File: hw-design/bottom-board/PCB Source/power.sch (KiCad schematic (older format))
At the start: 19 parts, among them J1 Power Jack, J2 HMI_POWER, U1 MURATA 5V, U2 LD1117S50TR_SOT223

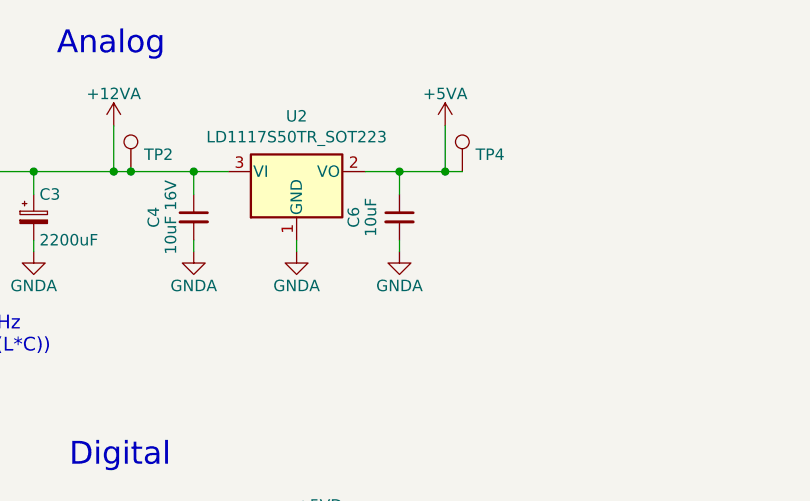
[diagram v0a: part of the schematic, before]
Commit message: change bias voltages to 5V, isolate input GND connections
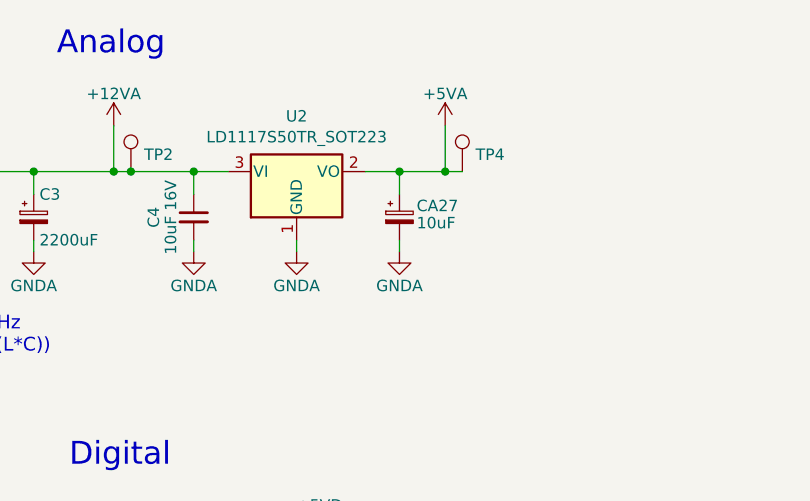
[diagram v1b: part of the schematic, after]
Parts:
- removed C6: 10uF, Capacitor_SMD:C_0603_1608Metric, symbol bottom-board-rescue:C_Small-Device
- added CA27: 10uF, Capacitor_SMD:CP_Elec_4x5.7, symbol bottom-board-rescue:CP_Small-Device
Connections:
- net +5VA: now also CA27.1
- net GND: now also CA27.2
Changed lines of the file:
@@
 Wire Wire Line
 	5900 1950 6100 1950
-$Comp
-L bottom-board-rescue:C_Small-Device C6
-U 1 1 5B5D1557
-P 5900 2150
-F 0 "C6" V 5700 2150 50  0000 C CNN
-F 1 "10uF" V 5775 2150 50  0000 C CNN
-F 2 "Capacitor_SMD:C_0603_1608Metric" H 5900 2150 60  0001 C CNN
-F 3 "" H 5900 2150 60  0000 C CNN
-F 4 "CL10A106MQ8NNNC" H 600 -3200 50  0001 C CNN "MPN"
-	1    5900 2150
-	1    0    0    -1
-$EndComp
 Text Notes 3650 2750 0    60   ~ 0
 LPF Fc=107Hz\n1/(2*pi*sqrt(L*C))
@@
 Wire Wire Line
 	8750 5300 8800 5300
+$Comp
+L bottom-board-rescue:CP_Small-Device CA?
+U 1 1 5FDC0C8E
+P 5900 2150
+AR Path="/54F72C8D/5FDC0C8E" Ref="CA?"  Part="1"
+AR Path="/54F7244B/5FDC0C8E" Ref="CA27"  Part="1"
+F 0 "CA27" H 5975 2200 50  0000 L CNN
+F 1 "10uF" H 5975 2125 50  0000 L CNN
+F 2 "Capacitor_SMD:CP_Elec_4x5.7" H 5900 2150 60  0001 C CNN
+F 3 "" H 5900 2150 60  0000 C CNN
+F 4 "EEE-HB1C100R" H 800 650 50  0001 C CNN "MPN"
+	1    5900 2150
+	1    0    0    -1
+$EndComp
 $EndSCHEMATC

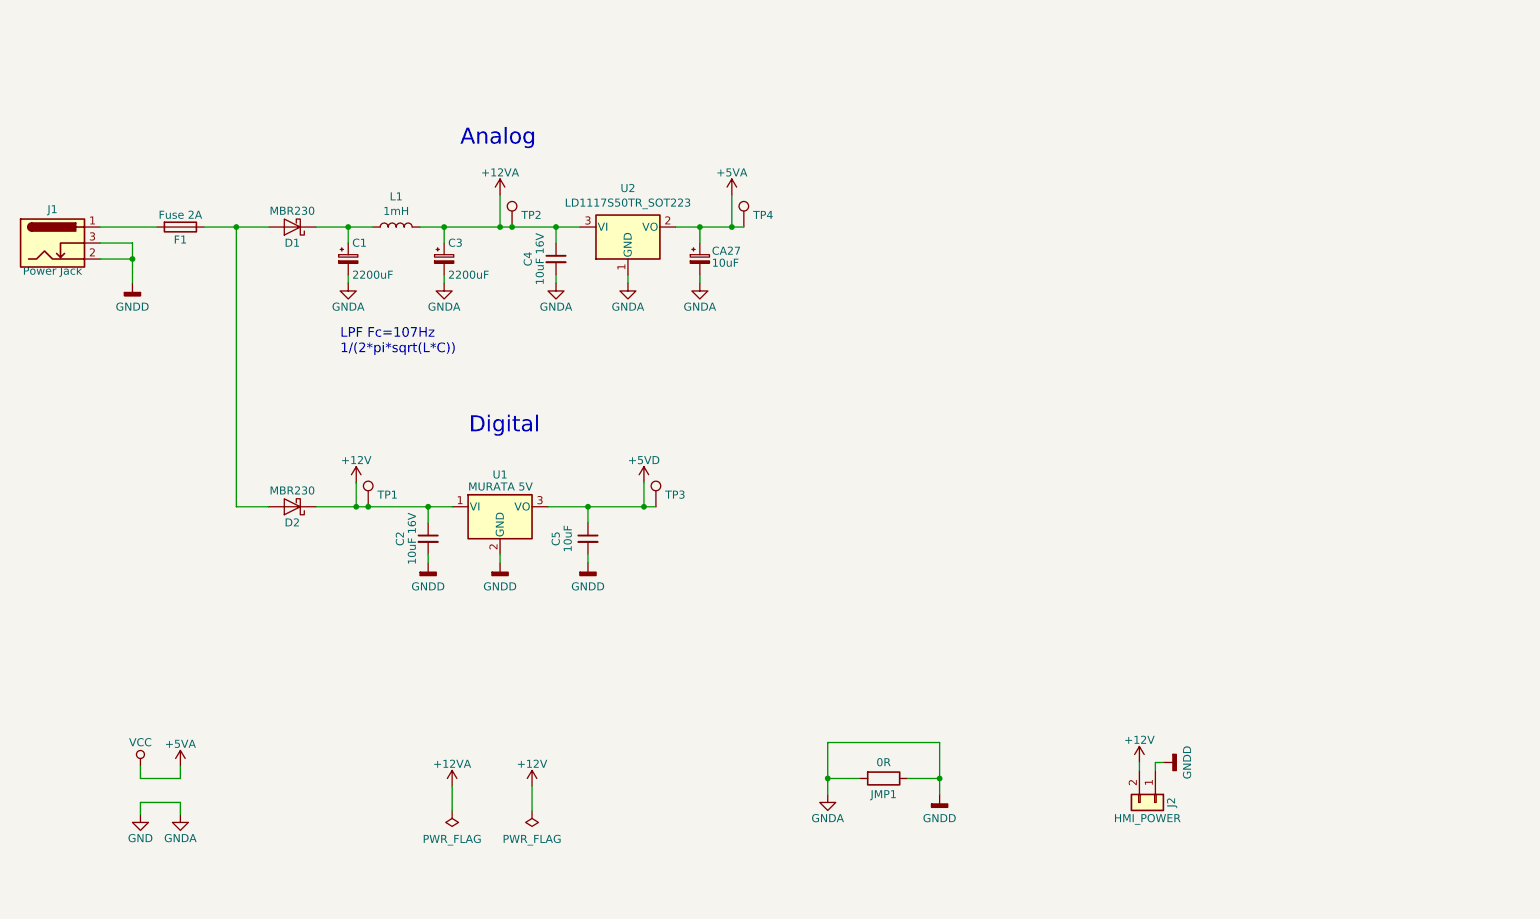
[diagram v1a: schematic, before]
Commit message: add docs + change pwr schematic
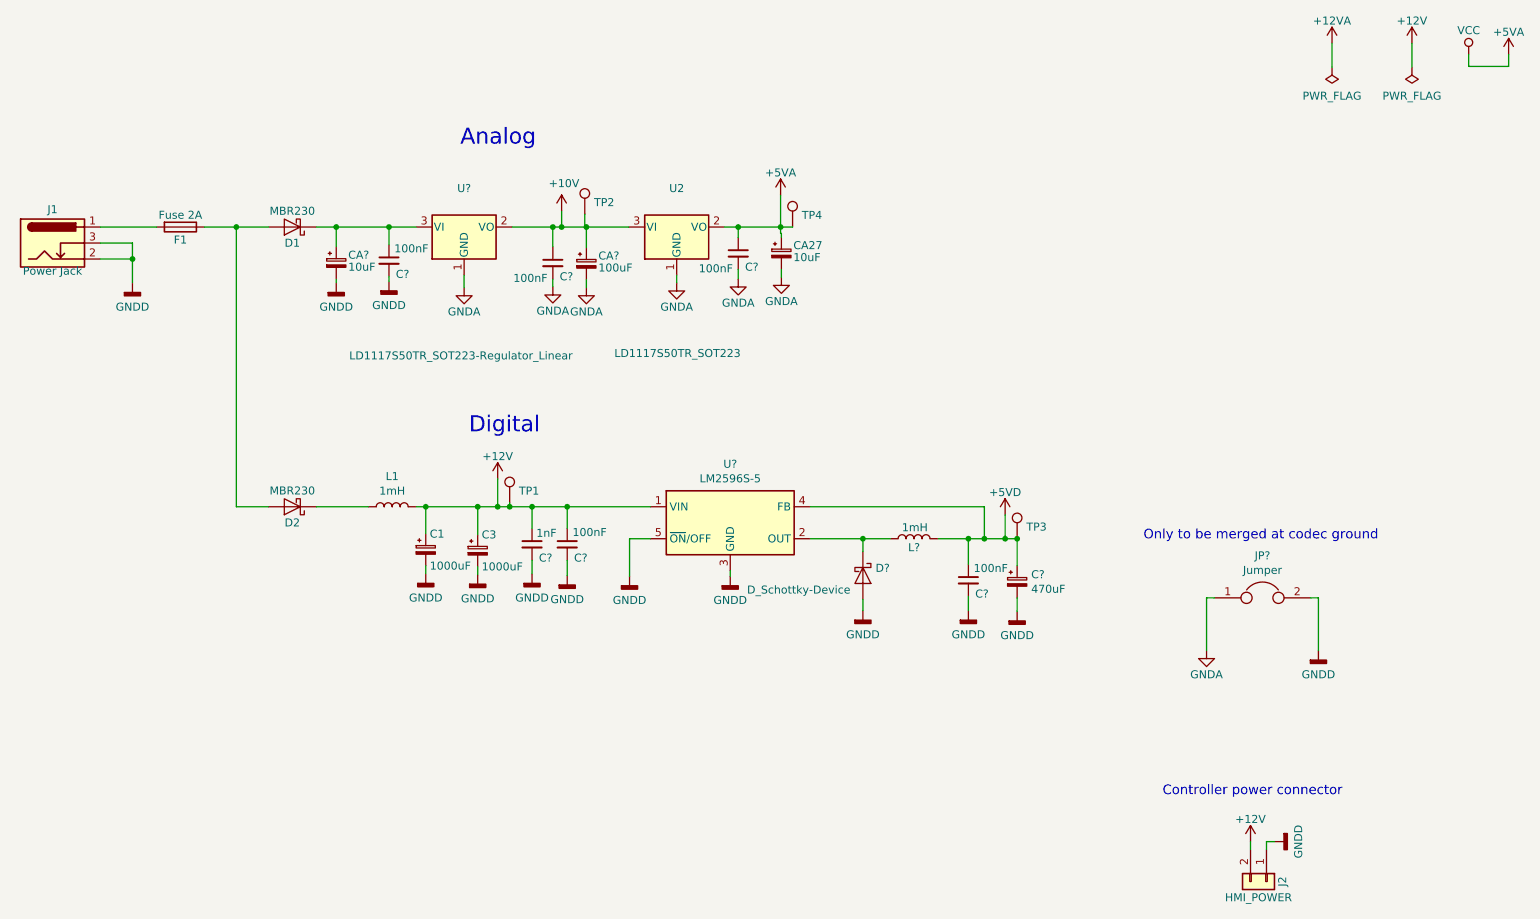
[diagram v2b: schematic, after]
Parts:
- removed C2, C4: 10uF 16V, Capacitor_SMD:C_0805_2012Metric, symbol bottom-board-rescue:C_Small-Device
- removed C5: 10uF, Capacitor_SMD:C_0603_1608Metric, symbol bottom-board-rescue:C_Small-Device
- removed JMP1: 0R, footprints:Jumper_SMD_THT, symbol bottom-board-rescue:R-Device
- removed U1: MURATA 5V, footprints:OKI-78SR_Vertical, symbol bottom-board-rescue:LM7805_TO220-Regulator_Linear
- added C?: 1nF, Capacitor_SMD:C_0603_1608Metric, symbol bottom-board-rescue:C_Small-Device
- added C? (x5): 100nF, Capacitor_SMD:C_0603_1608Metric, symbol bottom-board-rescue:C_Small-Device
- added C?: 470uF, Capacitor_SMD:CP_Elec_8x10.5, symbol Device:CP_Small
- added CA?: 10uF, Capacitor_SMD:CP_Elec_4x5.7, symbol bottom-board-rescue:CP_Small-Device
- added CA?: 100uF, Capacitor_SMD:CP_Elec_6.3x7.7, symbol bottom-board-rescue:CP_Small-Device
- added D?: D_Schottky-Device, symbol bottom-board-rescue:D_Schottky-Device
- added JP?: Jumper, symbol Device:Jumper
- added L?: 1mH, Inductor_SMD:L_Bourns_SRR1260, symbol bottom-board-rescue:L-Device
- added U?: LM2596S-5, Package_TO_SOT_SMD:TO-263-5_TabPin3, symbol Regulator_Switching:LM2596S-5
- added U?: LD1117S50TR_SOT223-Regulator_Linear, Package_TO_SOT_SMD:SOT-223-3_TabPin2, symbol bottom-board-rescue:LD1117S50TR_SOT223-Regulator_Linear
- C1, C3: value 2200uF -> 1000uF; footprint Capacitor_THT:CP_Radial_D10.0mm_P5.00mm -> Capacitor_SMD:CP_Elec_10x10.5; MPN 16PX2200MEFC10X20 -> UCM1C102MNL1GS
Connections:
- net +12V: now also C1.1, C3.1, L1.2, C?.1, C?.1, U?.1 (VIN); no longer D2.1 (K)
- net +12VA: no longer C3.1, L1.2, TP2.1, U2.3 (VI)
- net +5VA: now also C?.1
- net +5VD: now also C?.1, C?.1, L?.2, U?.4 (FB)
- net GND renamed GNDD
- net GNDD: now also C?.2, C?.2, C?.2, C?.2, C?.2, CA?.2, D?.2 (A), JP?.2, U?.3 (GND), U?.5 (~ON~/OFF); no longer CA27.2, U2.1 (GND)
- new net: C?.1, CA?.1, D1.1 (K), U?.3 (VI)
- new net: D2.1 (K), L1.1
- new net: D?.1 (K), L?.1, U?.2 (OUT)
- new net +10V: C?.1, CA?.1, TP2.1, U2.3 (VI), U?.2 (VO)
- new net GNDA: C?.2, C?.2, CA27.2, CA?.2, JP?.1, U2.1 (GND), U?.1 (GND)
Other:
- note added: "Controller power connector"
- note added: "Only to be merged at codec ground"
- note removed: "LPF Fc=107Hz\n1/(2*pi*sqrt(L*C))"
- moved on the sheet: C1, C3, CA27, J2, L1, TP1, TP2, TP3, TP4, U2

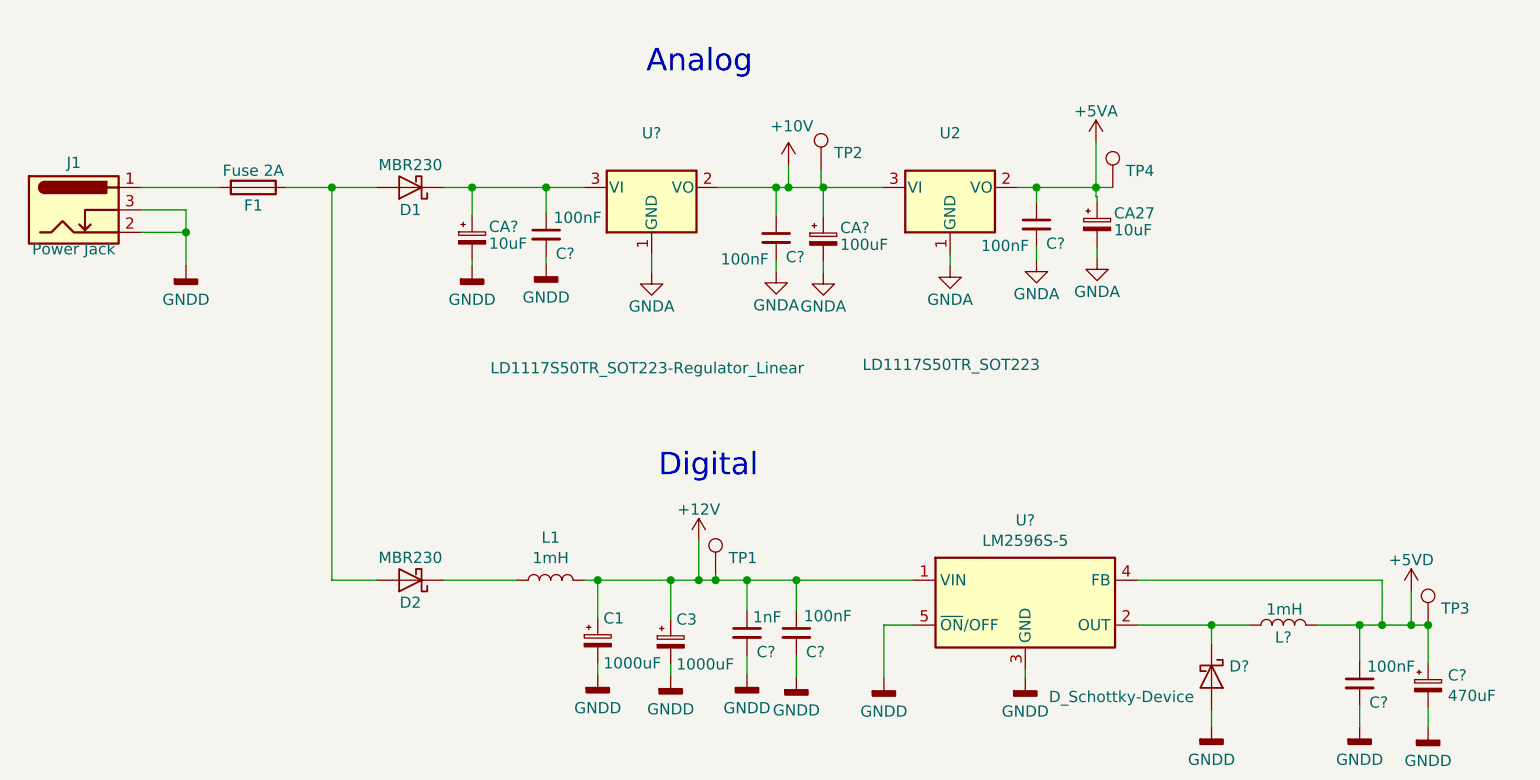
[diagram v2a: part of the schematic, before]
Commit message: match power circuit with the dwarf
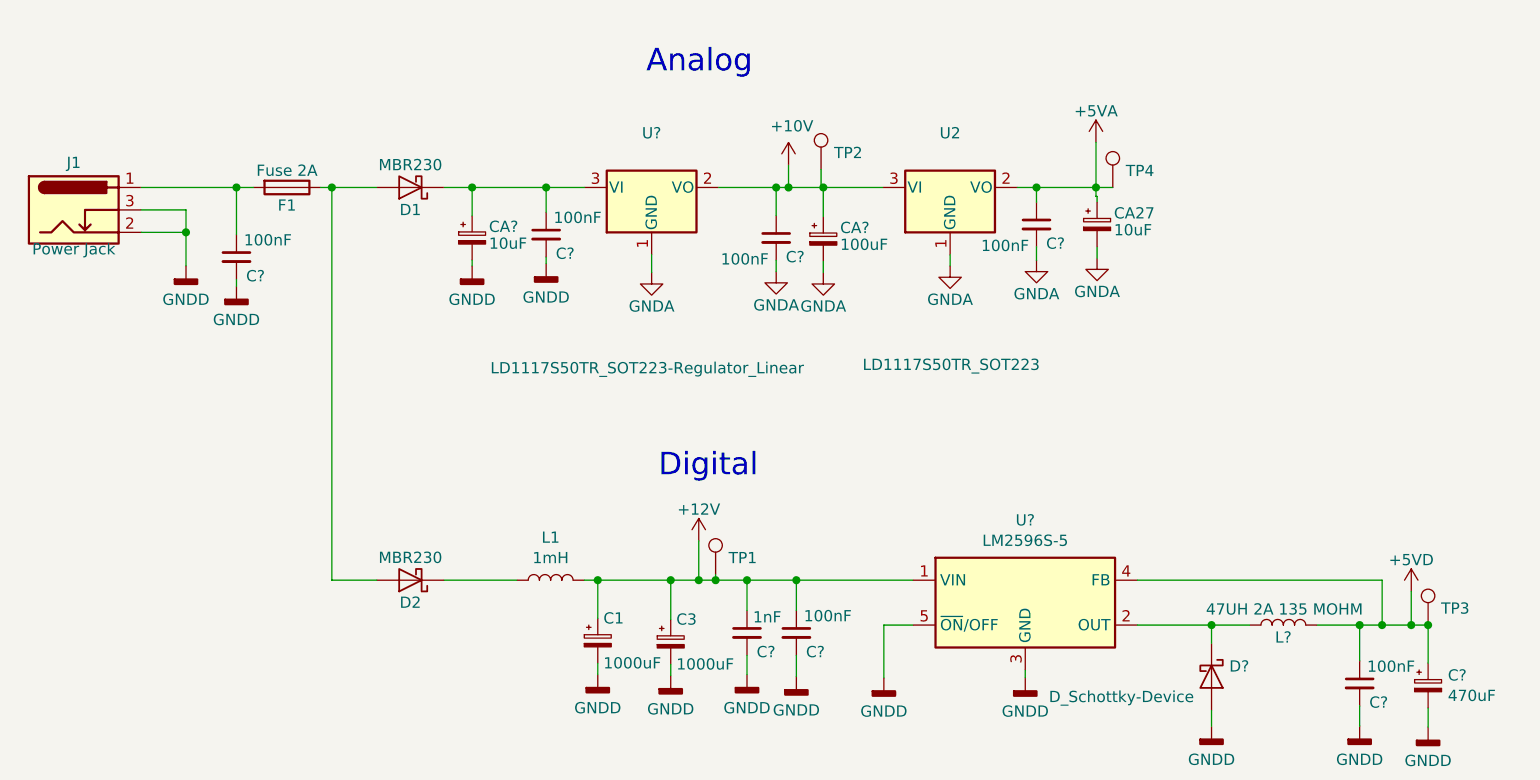
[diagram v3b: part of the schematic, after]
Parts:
- added C?: 100nF, Capacitor_SMD:C_0603_1608Metric, symbol bottom-board-rescue:C_Small-Device
- L?: value 1mH -> 47UH 2A 135 MOHM; footprint Inductor_SMD:L_Bourns_SRR1260 -> Uno:SRN8040TA; MPN SRR1260-102K -> SRN8040TA-470M
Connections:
- net GNDD: now also C?.2
- net at F1.2, J1.1: now also C?.1
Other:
- moved on the sheet: F1
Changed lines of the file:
@@
 Wire Wire Line
 	5190 2280 5190 2330
-Connection ~ 3000 1950
-Wire Wire Line
-	3000 3700 3000 1950
 Wire Wire Line
 	3200 3700 3000 3700
-Wire Wire Line
-	2800 1950 3000 1950
 Connection ~ 2350 2150
 Wire Wire Line
@@
 L bottom-board-rescue:Fuse-Device F1
 U 1 1 5B4F9399
-P 2650 1950
-F 0 "F1" V 2730 1950 50  0000 C CNN
-F 1 "Fuse 2A" V 2575 1950 50  0000 C CNN
-F 2 "footprints:Fuse_2920_0ZCF_Bel" V 2580 1950 50  0001 C CNN
-F 3 "" H 2650 1950 50  0001 C CNN
-F 4 "0ZCF0200FF2C" H 800 -1500 50  0001 C CNN "MPN"
-	1    2650 1950
+P 2800 1950
+F 0 "F1" V 2880 1950 50  0000 C CNN
+F 1 "Fuse 2A" V 2725 1950 50  0000 C CNN
+F 2 "footprints:Fuse_2920_0ZCF_Bel" V 2730 1950 50  0001 C CNN
+F 3 "" H 2800 1950 50  0001 C CNN
+F 4 "0ZCF0200FF2C" H 950 -1500 50  0001 C CNN "MPN"
+	1    2800 1950
 	0    1    1    0
 $EndComp
@@
 Wire Wire Line
 	7810 3900 7885 3900
-Wire Wire Line
-	2150 1950 2500 1950
 $Comp
 L bottom-board-rescue:VCC-power #PWR?
@@
 P 7240 3900
 F 0 "L?" V 7185 3900 50  0000 C CNN
-F 1 "1mH" V 7310 3895 50  0000 C CNN
-F 2 "Inductor_SMD:L_Bourns_SRR1260" H 7293 3809 50  0001 L CNN
+F 1 "47UH 2A 135 MOHM" V 7310 3895 50  0000 C CNN
+F 2 "Uno:SRN8040TA" H 7293 3809 50  0001 L CNN
 F 3 "" H 7240 3900 50  0000 C CNN
-F 4 "SRR1260-102K" H 7240 3900 60  0001 C CNN "MPN"
+F 4 "SRN8040TA-470M" H 7240 3900 60  0001 C CNN "MPN"
 	1    7240 3900
 	0    -1   -1   0
@@
 Wire Wire Line
 	5035 1950 5190 1950
+$Comp
+L bottom-board-rescue:C_Small-Device C?
+U 1 1 617E5398
+P 2575 2260
+F 0 "C?" H 2660 2175 50  0000 C CNN
+F 1 "100nF" H 2715 2335 50  0000 C CNN
+F 2 "Capacitor_SMD:C_0603_1608Metric" H 2575 2260 60  0001 C CNN
+F 3 "" H 2575 2260 60  0000 C CNN
+F 4 "GCM188R71C104KA37D" H -2725 -3090 50  0001 C CNN "MPN"
+	1    2575 2260
+	1    0    0    -1
+$EndComp
+$Comp
+L bottom-board-rescue:GNDD-power #PWR?
+U 1 1 617E539E
+P 2575 2390
+F 0 "#PWR?" H 2575 2140 50  0001 C CNN
+F 1 "GNDD" H 2575 2240 50  0000 C CNN
+F 2 "" H 2575 2390 60  0000 C CNN
+F 3 "" H 2575 2390 60  0000 C CNN
+	1    2575 2390
+	1    0    0    -1
+$EndComp
+Wire Wire Line
+	2575 2360 2575 2390
+Wire Wire Line
+	3000 1950 3000 3700
+Wire Wire Line
+	2150 1950 2575 1950
+Wire Wire Line
+	2950 1950 3000 1950
+Connection ~ 3000 1950
+Wire Wire Line
+	2575 2160 2575 1950
+Connection ~ 2575 1950
+Wire Wire Line
+	2575 1950 2650 1950
 $EndSCHEMATC

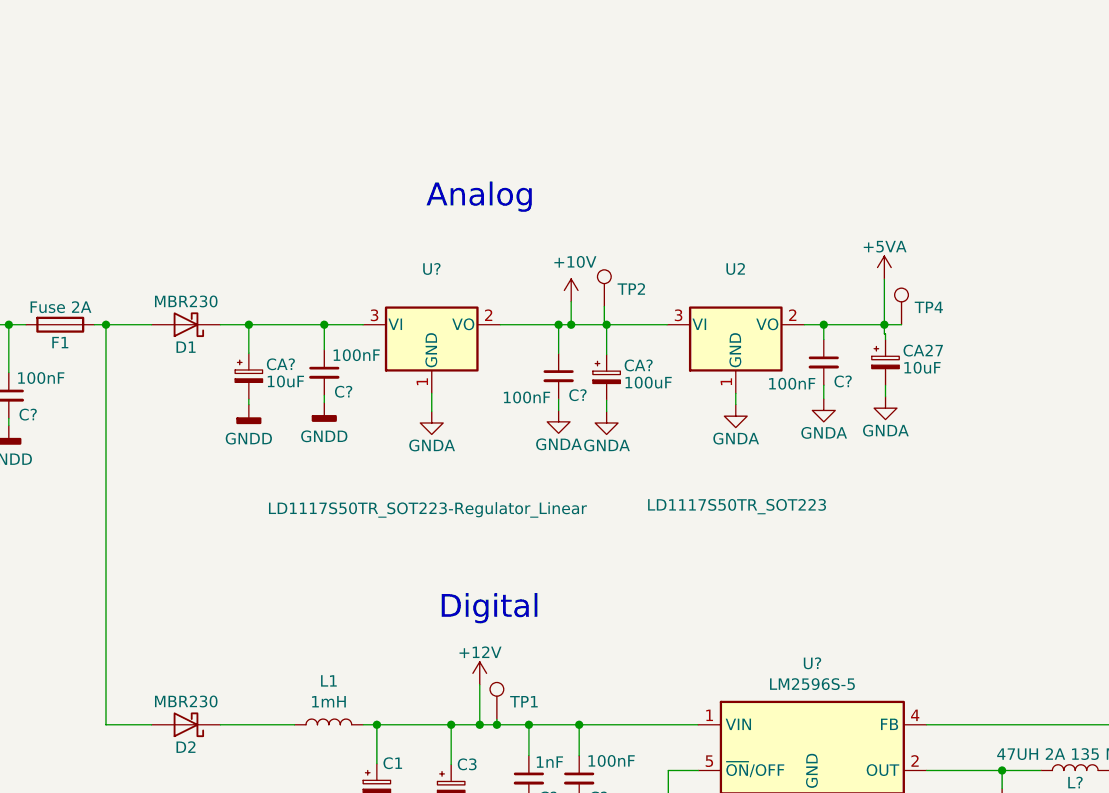
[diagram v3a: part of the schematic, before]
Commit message: improve codec filtering
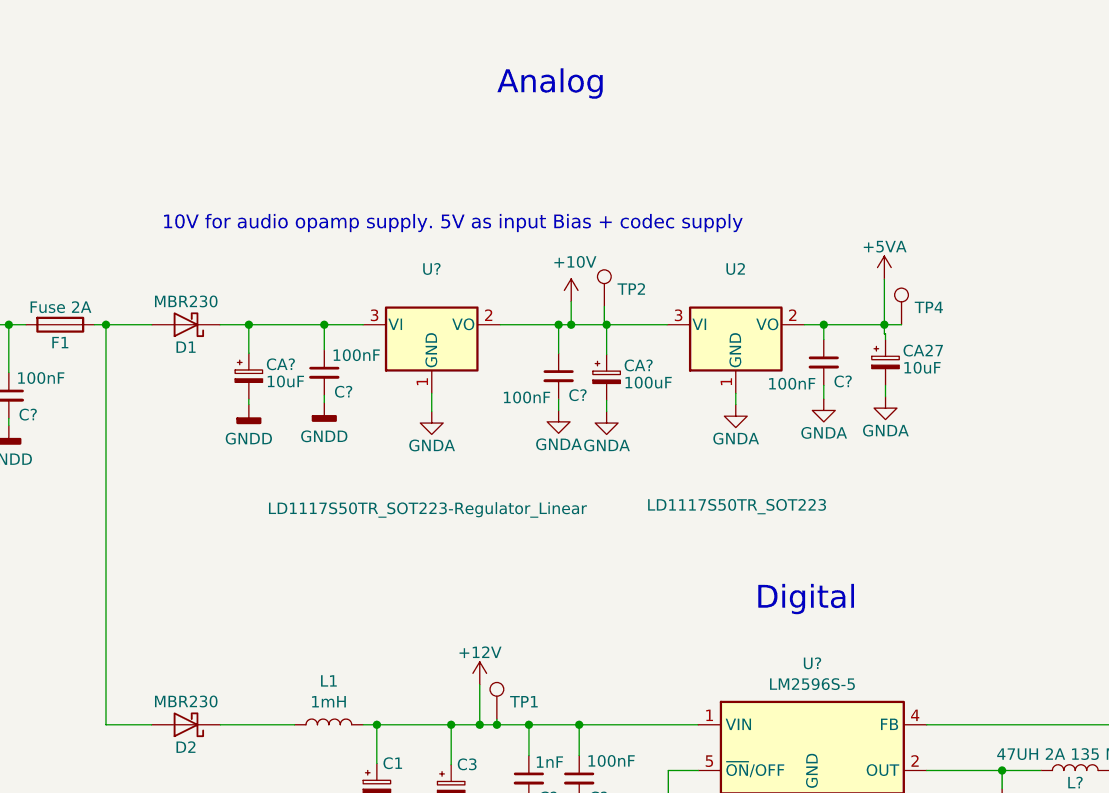
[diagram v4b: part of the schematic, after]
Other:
- note added: "10V for audio opamp supply. 5V as input Bias + codec supply"
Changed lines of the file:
@@
 	1    0    0    -1
 $EndComp
-Text Notes 4875 1450 2    100  ~ 0
+Text Notes 5185 955  2    100  ~ 0
 Analog
 $Comp
@@
 	0    1    1    0
 $EndComp
-Text Notes 4900 3250 2    100  ~ 0
+Text Notes 6285 3210 2    100  ~ 0
 Digital
 Wire Wire Line
@@
 Wire Wire Line
 	2575 1950 2650 1950
+Text Notes 3245 1545 0    60   ~ 0
+10V for audio opamp supply. 5V as input Bias + codec supply
 $EndSCHEMATC
